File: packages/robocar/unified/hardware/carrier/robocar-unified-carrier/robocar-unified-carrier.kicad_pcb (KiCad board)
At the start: 2 copper layers, 100 x 100 mm, 38 parts, among them J1 IDC 2x7 head cable, J10 Piezo, J2 IDC 2x7 head cable, J3 XT30 pack in, J4 LM2596 module, J5 Motor left, J6 Motor right, J7 RCWL-1601 front, J8 RCWL-1601 rear, J9 SSD1306 0.91in, U1 XIAO ESP32-S3 Sense, U2 AMS1117-3.3

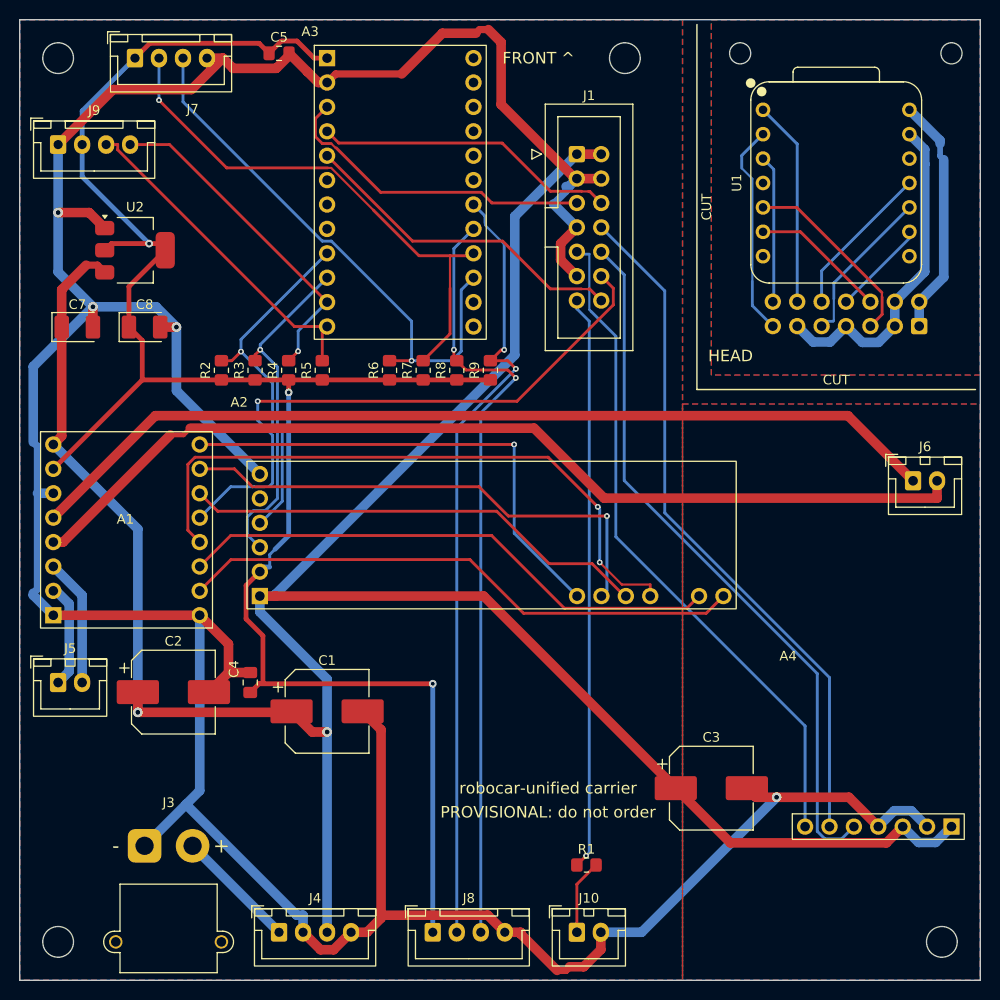
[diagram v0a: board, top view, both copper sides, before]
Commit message: fix(robocar-unified): fit the head board to the 30 x 30 mm cradle
Lauri measured the cradle's inner height at 30.0 mm as well as its width,
so the head is sawn to 29.5 x 29.5 mm: copper x 72-100, y 0-28, with the
3 mm band and saw lines at x 70.5 and y 29.5.

The XIAO socket and the shrouded IDC header (26.5 mm long) no longer fit
together in 28 mm, with or without the M2 holes. Lauri's choice: J2 and J1
become unshrouded 2x7 pin headers (one registry entry serves both ends),
J2 on the back face beside the XIAO, and the M2 holes go in the two bottom
corners. The ribbon plug is unkeyed on a pin header; the footprint's pin-1
mark carries the orientation on both faces.

HEAD_+5V and HEAD_GND move to the 0.5 mm logic_power class: 1 mm tracks
do not route between the head's pads, and the XIAO and camera draw well
under 1 A. Freerouting also routed head tracks onto the edge, inside
KiCad's 0.5 mm copper-to-edge rule, so 0.5 mm keepouts now line the top,
left and right edges (not the bottom, where J3's courtyard meets it).
The band's move frees the main board's corner, so A2 and C4 return to
their #794 positions.

Board re-placed and re-routed with carrier-board; carrier-check passes
and wrote the stamp. Still provisional: do not order.

Co-Authored-By: Claude Opus 5.5 <noreply@anthropic.com>
Claude-Session: https://claude.ai/code/session_01LmLtwHDbHDLXFMLxCn3smf
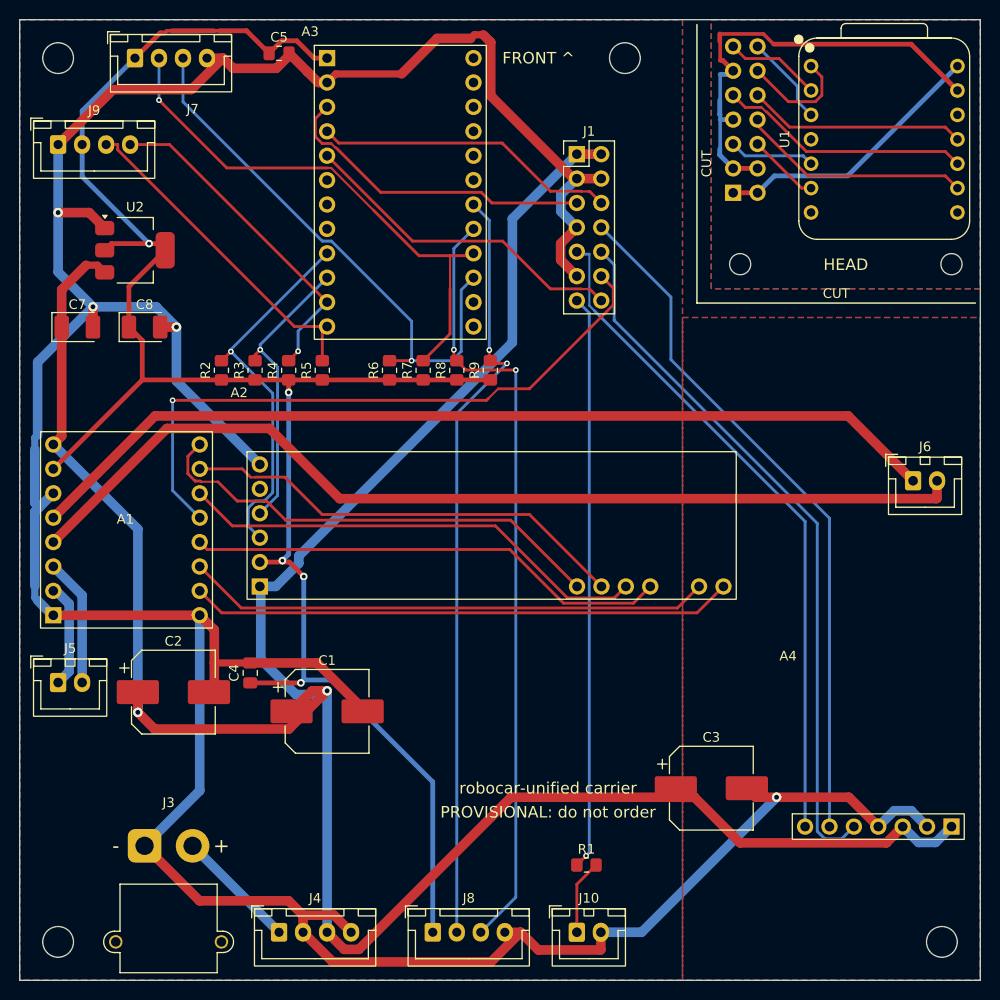
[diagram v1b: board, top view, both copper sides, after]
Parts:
- J1, J2: footprint Connector_IDC:IDC-Header_2x07_P2.54mm_Vertical -> Connector_PinHeader_2.54mm:PinHeader_2x07_P2.54mm_Vertical
- moved J2 23.8 mm to (174.3, 118.0), turned to 0 degrees
- moved H5 22.0 mm to (175.0, 125.5)
- moved H6 22.0 mm to (197.0, 125.5)
- moved U1 6.76 mm to (190.0, 112.5)
- moved A2 1.00 mm to (125.0, 159.0)
- moved C4 1.00 mm to (124.0, 168.0)
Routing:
- net BIN1: track 67.0 -> 50.3 mm, vias 2 -> 0
- net HEAD_I2S_BCLK: track 10.0 -> 24.1 mm
- net HEAD_GND: track 34.9 -> 47.6 mm
- net HEAD_PIEZO: track 22.2 -> 10.0 mm
- net HEAD_I2C_SDA: track 20.1 -> 8.96 mm
- net HEAD_I2S_LRCLK: track 16.6 -> 26.3 mm
- net HEAD_MOTOR_STBY: track 21.5 -> 11.8 mm
- net HEAD_I2C_SCL: track 14.2 -> 7.47 mm
- net HEAD_I2S_DIN: track 16.1 -> 22.7 mm
- net AIN2: track 53.0 -> 46.9 mm, vias 1 -> 0
- net HEAD_MUX_RST: track 15.4 -> 9.44 mm
- net +3V3: track 198.4 -> 194.1 mm, vias 3 -> 5
- net MOTOR_STBY: track 62.9 -> 66.9 mm
- net HEAD_+5V: track 25.1 -> 28.8 mm
- net GND: track 363.6 -> 360.8 mm
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
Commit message: fix(robocar-unified): put the head's M2 holes in its top corners
Lauri: the cradle's screws need to be near the head's top corners, where
there is room to drill for M2 heat-set inserts. H5 and H6 move there,
22.5 mm apart, as near the corners as the 0.5 mm edge keepout and the cut
band allow; the USB-C sits between them. U1 and J2 move down below them.
The PCB holes stay 2.2 mm M2 clearance; the inserts go in the cradle.

Board re-placed and re-routed with carrier-board; carrier-check passes
and wrote the stamp. Still provisional: do not order.

Co-Authored-By: Claude Opus 5.5 <noreply@anthropic.com>
Claude-Session: https://claude.ai/code/session_01LmLtwHDbHDLXFMLxCn3smf
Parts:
- moved H5 22.4 mm to (174.5, 103.0)
- moved H6 22.4 mm to (197.0, 103.0)
- moved J2 4.60 mm to (174.3, 122.6)
- moved U1 3.75 mm to (190.0, 116.2)
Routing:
- net HEAD_+5V: track 28.8 -> 39.1 mm
- net HEAD_GND: track 47.6 -> 40.3 mm
- net HEAD_MUX_RST: track 9.44 -> 8.59 mm
- net HEAD_I2S_BCLK: track 24.1 -> 23.4 mm
